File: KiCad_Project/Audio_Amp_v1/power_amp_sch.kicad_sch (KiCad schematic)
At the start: 44 parts, among them IC2 TPA3116D2DAD

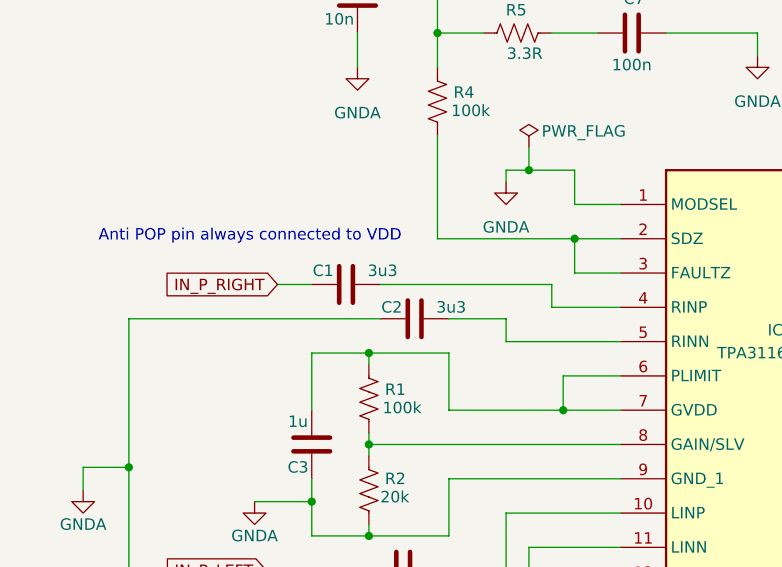
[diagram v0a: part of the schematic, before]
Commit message: schematic update
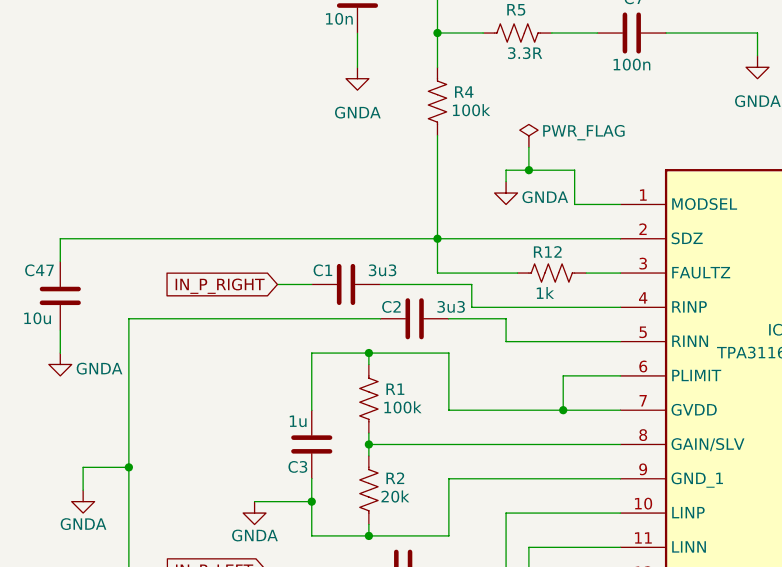
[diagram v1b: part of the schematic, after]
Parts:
- added C47: 10u, Capacitor_SMD:C_0603_1608Metric, symbol Device:C
- added R12: 1k, Resistor_SMD:R_0603_1608Metric, symbol Device:R_US
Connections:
- net GNDA: now also C47.1
- net at IC2.2 (SDZ), R4.2: now also C47.2, R12.1; no longer IC2.3 (FAULTZ)
- new net: IC2.3 (FAULTZ), R12.2
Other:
- note removed: "Anti POP pin always connected to VDD"

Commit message: Started routing
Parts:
- C39, C41: footprint EEE-FK1H221GV:EEHZT1E561UV -> Capacitor_SMD:CP_Elec_10x10.5; LCSC C116211 -> EEE-FN1V471UL
- C47: value 10u -> 47u; footprint Capacitor_SMD:C_0603_1608Metric -> Capacitor_SMD:CP_Elec_6.3x5.9; LCSC C5199872 -> EEE-FK1V470P
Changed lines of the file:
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@@
 			)
 		)
-		(property "Footprint" "EEE-FK1H221GV:EEHZT1E561UV"
+		(property "Footprint" "Capacitor_SMD:CP_Elec_10x10.5"
 			(at 171.45 146.05 0)
 			(hide yes)
@@
 			)
 		)
-		(property "Datasheet" "kicad-embed://ABA0000C1181.pdf"
+		(property "Datasheet" "https://industrial.panasonic.com/cdbs/www-data/pdf/RDE0000/RDE0000C1266.pdf"
 			(at 171.45 146.05 0)
 			(hide yes)
@@
 			)
 		)
-		(property "LCSC" "C116211"
+		(property "LCSC" "EEE-FN1V471UL "
 			(at 171.45 146.05 0)
 			(hide yes)
@@
 			)
 		)
-		(property "Value" "10u"
+		(property "Value" "47u"
 			(at 29.21 86.36 0)
 			(show_name no)
@@
 			)
 		)
-		(property "Footprint" "Capacitor_SMD:C_0603_1608Metric"
+		(property "Footprint" "Capacitor_SMD:CP_Elec_6.3x5.9"
 			(at 30.7848 80.01 0)
 			(hide yes)
@@
 			)
 		)
-		(property "Datasheet" ""
+		(property "Datasheet" "https://industrial.panasonic.com/cdbs/www-data/pdf/RDE0000/ABA0000C1181.pdf"
 			(at 31.75 83.82 0)
 			(hide yes)
@@
 			)
 		)
-		(property "LCSC" "C5199872"
+		(property "LCSC" "EEE-FK1V470P"
 			(at 31.75 83.82 90)
 			(hide yes)
@@
 			)
 		)
-		(property "Footprint" "EEE-FK1H221GV:EEHZT1E561UV"
+		(property "Footprint" "Capacitor_SMD:CP_Elec_10x10.5"
 			(at 173.99 49.53 0)
 			(hide yes)
@@
 			)
 		)
-		(property "Datasheet" "kicad-embed://ABA0000C1181.pdf"
+		(property "Datasheet" "https://industrial.panasonic.com/cdbs/www-data/pdf/RDE0000/RDE0000C1266.pdf"
 			(at 173.99 49.53 0)
 			(hide yes)
@@
 			)
 		)
-		(property "LCSC" "C116211"
+		(property "LCSC" "EEE-FN1V471UL"
 			(at 173.99 49.53 0)
 			(hide yes)

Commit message: added reverse polarity protection
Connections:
- net GNDA: now also C1.1, C4.2; no longer C2.1, C5.2
- net IN_P_LEFT: now also C5.2; no longer C4.2
- net IN_P_RIGHT: now also C2.1; no longer C1.1
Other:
- note added: "Due to inversion of the OPAMP I switched the phase of the TPA inputs"
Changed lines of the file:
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@@
+		)
+	)
+	(text "Due to inversion of the OPAMP\nI switched the phase of the TPA inputs\n"
+		(exclude_from_sim no)
+		(at 43.688 73.406 0)
+		(effects
+			(font
+				(size 1.27 1.27)
+			)
 		)
 	)
@@
 	(wire
 		(pts
+			(xy 66.04 114.3) (xy 39.37 114.3)
+		)
+		(stroke
+			(width 0)
+			(type default)
+		)
+	)
+	(wire
+		(pts
 			(xy 163.83 55.88) (xy 163.83 53.34)
 		)
@@
 	(wire
 		(pts
-			(xy 39.37 102.87) (xy 39.37 118.11)
+			(xy 39.37 102.87) (xy 39.37 114.3)
 		)
 		(stroke
@@
 	(wire
 		(pts
-			(xy 39.37 86.36) (xy 67.31 86.36)
-		)
-		(stroke
-			(width 0)
-			(type default)
-		)
-	)
-	(wire
-		(pts
 			(xy 73.66 81.28) (xy 73.66 77.47)
 		)
@@
 	(wire
 		(pts
+			(xy 58.42 86.36) (xy 67.31 86.36)
+		)
+		(stroke
+			(width 0)
+			(type default)
+		)
+	)
+	(wire
+		(pts
 			(xy 153.67 152.4) (xy 162.56 152.4)
 		)
@@
 	(wire
 		(pts
-			(xy 59.69 82.55) (xy 55.88 82.55)
-		)
-		(stroke
-			(width 0)
-			(type default)
-		)
-	)
-	(wire
-		(pts
 			(xy 214.63 68.58) (xy 214.63 77.47)
 		)
@@
 	(wire
 		(pts
-			(xy 39.37 86.36) (xy 39.37 102.87)
+			(xy 39.37 82.55) (xy 39.37 102.87)
 		)
 		(stroke
@@
 	(wire
 		(pts
-			(xy 39.37 118.11) (xy 58.42 118.11)
-		)
-		(stroke
-			(width 0)
-			(type default)
-		)
-	)
-	(wire
-		(pts
 			(xy 64.77 44.45) (xy 64.77 46.99)
 		)
@@
 	(wire
 		(pts
-			(xy 54.61 114.3) (xy 66.04 114.3)
+			(xy 39.37 82.55) (xy 59.69 82.55)
 		)
 		(stroke
@@
 	(global_label "IN_P_RIGHT"
 		(shape input)
-		(at 55.88 82.55 180)
+		(at 58.42 86.36 180)
 		(fields_autoplaced yes)
 		(effects
@@
 		)
 		(property "Intersheetrefs" "${INTERSHEET_REFS}"
-			(at 42.3114 82.55 0)
+			(at 44.8514 86.36 0)
 			(hide yes)
 			(show_name no)
@@
 	(global_label "IN_P_LEFT"
 		(shape input)
-		(at 54.61 114.3 180)
+		(at 58.42 118.11 180)
 		(fields_autoplaced yes)
 		(effects
@@
 		)
 		(property "Intersheetrefs" "${INTERSHEET_REFS}"
-			(at 42.251 114.3 0)
+			(at 46.061 118.11 0)
 			(hide yes)
 			(show_name no)

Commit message: Added led into pcb and lyout completed
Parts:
- C1, C2, C4, C5: LCSC C5199872 -> C445723
- C39, C41: LCSC EEE-FN1V471UL -> C46550413
- C47: LCSC EEE-FK1V470P -> C7469958
- L1, L2, L3, L4: LCSC (none) -> C55539373
- R1, R4: LCSC C2907088 -> C14675
- R12: LCSC C2907088 -> C22548

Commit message: Use shared Kicad_Libs instead of project-specific libraries
- Project parts moved to Kicad_Libs (symbol, footprint, 3D, datasheet)
- Lib tables point to ${KIPRJMOD}/../KiCad_Libs (link via bring_libs.bat)
- Schematic/PCB references (lib ids, footprints, 3D paths, datasheets)
  updated to the Kicad_Libs libraries; no design changes
- Removed the old project-specific library folder
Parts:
- C10, C17: footprint EEE-FK1H221GV:EEHZT1E561UV -> eCapacitor:EEHZT1E561UV
- IC2: footprint TPA3116D2DAD:SOP65P810X120-32N -> eAmplifier:SOP65P810X120-32N; symbol TPA3116D2DAD:TPA3116D2DAD -> eAmplifier:TPA3116D2DAD
- L1, L2, L3, L4: footprint 7443341000:INDPM8479X720N -> eCoil:INDPM8479X720N
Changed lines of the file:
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@@
 			)
 		)
-		(property "Footprint" "7443341000:INDPM8479X720N"
+		(property "Footprint" "eCoil:INDPM8479X720N"
 			(at 193.04 152.4 0)
 			(hide yes)
@@
 			)
 		)
-		(property "Datasheet" "kicad-embed://7443341000.pdf"
+		(property "Datasheet" "${KIPRJMOD}/../KiCad_Libs/eCoil/datasheet/7443341000.pdf"
 			(at 193.04 152.4 0)
 			(hide yes)
@@
 			)
 		)
-		(property "Footprint" "EEE-FK1H221GV:EEHZT1E561UV"
+		(property "Footprint" "eCapacitor:EEHZT1E561UV"
 			(at 163.83 49.53 0)
 			(hide yes)
@@
 			)
 		)
-		(property "Datasheet" "kicad-embed://ABA0000C1181.pdf"
+		(property "Datasheet" "${KIPRJMOD}/../KiCad_Libs/eCapacitor/datasheet/ABA0000C1181.pdf"
 			(at 163.83 49.53 0)
 			(hide yes)
@@
 			)
 		)
-		(property "Footprint" "7443341000:INDPM8479X720N"
+		(property "Footprint" "eCoil:INDPM8479X720N"
 			(at 193.04 104.14 0)
 			(hide yes)
@@
 			)
 		)
-		(property "Datasheet" "kicad-embed://7443341000.pdf"
+		(property "Datasheet" "${KIPRJMOD}/../KiCad_Libs/eCoil/datasheet/7443341000.pdf"
 			(at 193.04 104.14 0)
 			(hide yes)
@@
 			)
 		)
-		(property "Footprint" "7443341000:INDPM8479X720N"
+		(property "Footprint" "eCoil:INDPM8479X720N"
 			(at 193.04 44.45 0)
 			(hide yes)
@@
 			)
 		)
-		(property "Datasheet" "kicad-embed://7443341000.pdf"
+		(property "Datasheet" "${KIPRJMOD}/../KiCad_Libs/eCoil/datasheet/7443341000.pdf"
 			(at 193.04 44.45 0)
 			(hide yes)
@@
 			)
 		)
-		(property "Footprint" "7443341000:INDPM8479X720N"
+		(property "Footprint" "eCoil:INDPM8479X720N"
 			(at 193.04 92.71 0)
 			(hide yes)
@@
 			)
 		)
-		(property "Datasheet" "kicad-embed://7443341000.pdf"
+		(property "Datasheet" "${KIPRJMOD}/../KiCad_Libs/eCoil/datasheet/7443341000.pdf"
 			(at 193.04 92.71 0)
 			(hide yes)
@@
 	)
 	(symbol
-		(lib_id "TPA3116D2DAD:TPA3116D2DAD")
+		(lib_id "eAmplifier:TPA3116D2DAD")
 		(at 93.98 95.25 0)
 		(unit 1)
@@
 			)
 		)
-		(property "Footprint" "TPA3116D2DAD:SOP65P810X120-32N"
+		(property "Footprint" "eAmplifier:SOP65P810X120-32N"
 			(at 125.73 190.17 0)
 			(hide yes)
@@
 			)
 		)
-		(property "Datasheet" "kicad-embed://tpa3116d2.pdf"
+		(property "Datasheet" "${KIPRJMOD}/../KiCad_Libs/eAmplifier/datasheet/tpa3116d2.pdf"
 			(at 125.73 290.17 0)
 			(hide yes)
@@
 			)
 		)
-		(property "Footprint" "EEE-FK1H221GV:EEHZT1E561UV"
+		(property "Footprint" "eCapacitor:EEHZT1E561UV"
 			(at 162.56 146.05 0)
 			(hide yes)
@@
 			)
 		)
-		(property "Datasheet" "kicad-embed://ABA0000C1181.pdf"
+		(property "Datasheet" "${KIPRJMOD}/../KiCad_Libs/eCapacitor/datasheet/ABA0000C1181.pdf"
 			(at 162.56 146.05 0)
 			(hide yes)
